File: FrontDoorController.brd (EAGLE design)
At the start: 31.4 x 49.1 mm, 11 parts

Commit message: Door_Control_PCB: Add SW3 and SW4 from Lockitron
The Lockitron has 4 limit switches instead of 2 like I originally
thought.  They also need a common place to wire their NC connections to
and with this many switches it seemed best to give them their own header
row, causing some other components to have to move and some other pins
to need moving as well.  Things all seem to flow well now and there
should be plenty of power to all of the components.
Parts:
- removed R1: 1K, SparkFun-Resistors:0603-RES
- added JP2: (no value), SparkFun-Connectors:1X04_LOCK
- moved D1 8.62 mm to (7.05, 6.98)
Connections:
- removed net A0: PHOTON.12, U$3.12
- removed net A1: PHOTON.11, U$3.11
- removed net VM: C1.A, C2.1, D1.A, JP1.6, U$2.13, U$2.14, U$2.24
- new net SW3: JP2.1, PHOTON.12, U$3.12
- new net SW4: JP2.2, PHOTON.11, U$3.11
- new net VBAK: PHOTON.22, U$3.22
- net DOORSW: no longer R1.2
- net GND: now also JP1.8, JP1.9; no longer R1.1
- net SW1: now also JP2.3; no longer JP1.8
- net SW2: now also JP2.4; no longer JP1.9
- net VBAT: now also C1.A, C2.1, D1.A, JP1.6, U$2.13, U$2.14, U$2.24; no longer PHOTON.22, U$3.22
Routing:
- net SW4: track 0.00 -> 33.2 mm, vias 0 -> 1
- net SW3: track 0.00 -> 22.4 mm
- net VM: track 14.2 -> 0.00 mm, vias 2 -> 0
- net VBAT: track 1.40 -> 14.2 mm, vias 0 -> 2
- net SW1: track 17.2 -> 12.1 mm
- net VIN: track 72.1 -> 76.6 mm
- net SW2: track 18.7 -> 15.5 mm
- net VBAK: track 0.00 -> 1.40 mm
- net A1: track 1.40 -> 0.00 mm
- net A0: track 1.38 -> 0.00 mm
- net DOORSW: track 25.0 -> 24.0 mm
- added copper zone on layer 1, net VBAT
- removed copper zone on layer 1, net VM
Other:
- board text added: "Door COM"
- board text added: "Door NC"
- board text added: "SW NC"
- board text added: "SW3"
- board text added: "SW4"
- board text added: "VBAT"
- board text removed: "DOORSW"
- board text removed: "VM"

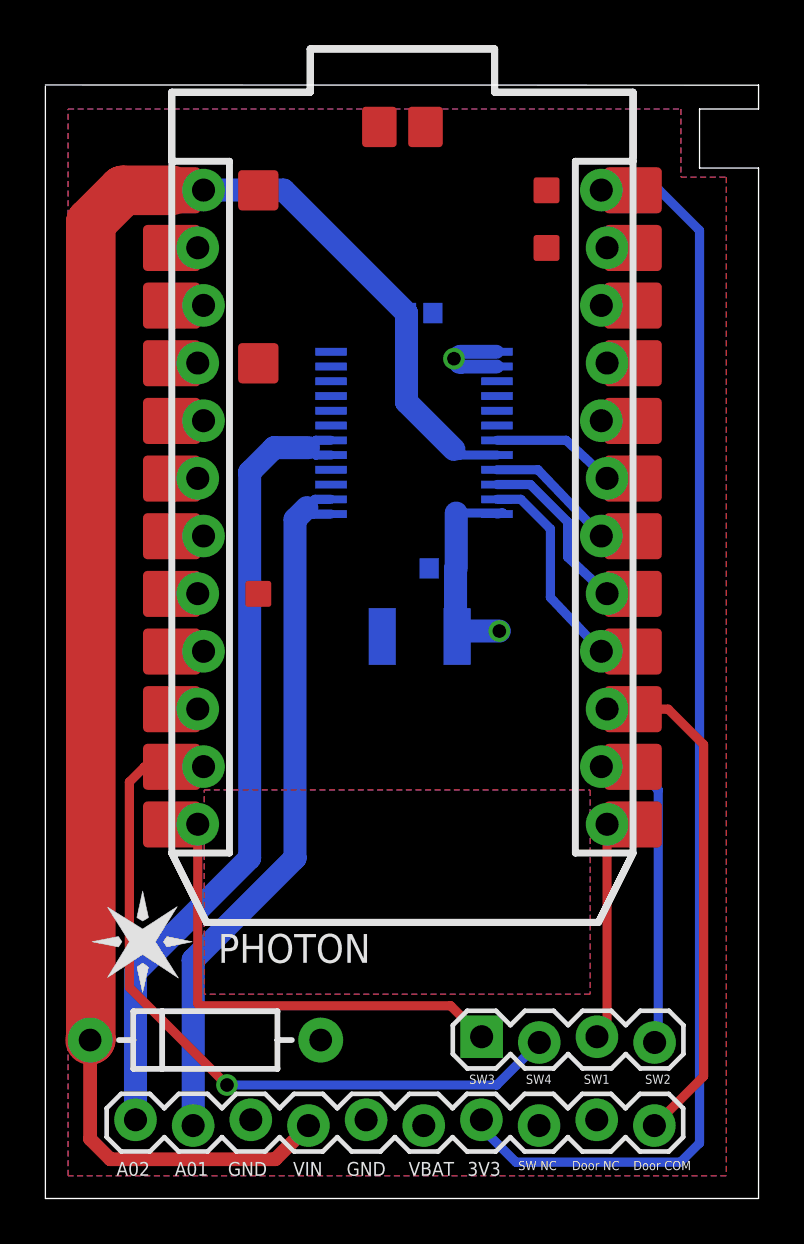
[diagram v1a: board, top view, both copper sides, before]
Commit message: Door_Control_PCB: Widen Motor A01/2 traces
These were probably wide enough but I thought that giving them as much
surface area as possible to transmit high current to the motor is a good
thing so I widened the traces by a bit.  This also made the connections
to the IC pads much prettier.
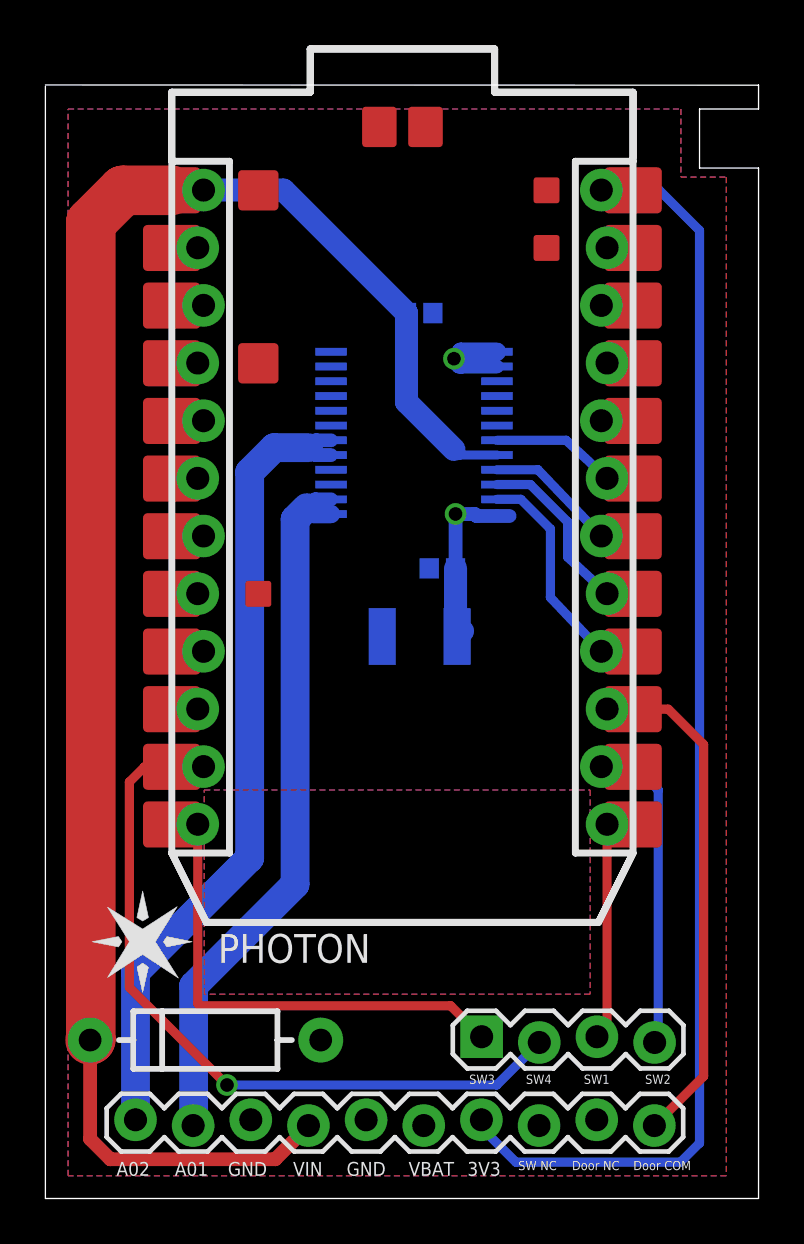
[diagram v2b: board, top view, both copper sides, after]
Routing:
- net VBAT: track 14.2 -> 13.2 mm
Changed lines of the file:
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@@
 <contactref element="U$2" pad="2"/>
 <contactref element="JP1" pad="2"/>
-<wire x1="12.584" y1="30.805" x2="11.885" y2="30.805" width="0.4064" layer="16"/>
-<wire x1="11.885" y1="30.805" x2="11.52" y2="30.44" width="0.4064" layer="16"/>
+<wire x1="12.584" y1="30.805" x2="11.885" y2="30.805" width="0.6096" layer="16"/>
+<wire x1="11.885" y1="30.805" x2="11.52" y2="30.44" width="0.6096" layer="16"/>
 <wire x1="11.52" y1="30.44" x2="11.805" y2="30.155" width="0.4064" layer="16"/>
-<wire x1="11.805" y1="30.155" x2="12.584" y2="30.155" width="0.4064" layer="16"/>
-<wire x1="6.51" y1="3.213" x2="6.51" y2="10.51" width="1.016" layer="16"/>
-<wire x1="6.51" y1="10.51" x2="11" y2="15" width="1.016" layer="16"/>
-<wire x1="11" y1="15" x2="11" y2="29.92" width="1.016" layer="16"/>
-<wire x1="11" y1="29.92" x2="11.52" y2="30.44" width="1.016" layer="16"/>
+<wire x1="11.805" y1="30.155" x2="12.584" y2="30.155" width="0.8128" layer="16"/>
+<wire x1="11" y1="13.84" x2="11" y2="29.92" width="1.27" layer="16"/>
+<wire x1="11" y1="29.92" x2="11.52" y2="30.44" width="1.27" layer="16"/>
+<wire x1="11" y1="13.84" x2="6.53" y2="9.37" width="1.27" layer="16"/>
+<wire x1="6.53" y1="9.37" x2="6.53" y2="3.233" width="1.27" layer="16"/>
+<wire x1="6.53" y1="3.233" x2="6.51" y2="3.213" width="1.27" layer="16"/>
 </signal>
 <signal name="A02">
@@
 <contactref element="U$2" pad="6"/>
 <contactref element="JP1" pad="1"/>
-<wire x1="12.584" y1="32.755" x2="11.915" y2="32.755" width="0.4064" layer="16"/>
-<wire x1="11.915" y1="32.755" x2="11.59" y2="33.08" width="0.4064" layer="16"/>
-<wire x1="11.59" y1="33.08" x2="11.915" y2="33.405" width="0.4064" layer="16"/>
-<wire x1="11.915" y1="33.405" x2="12.584" y2="33.405" width="0.4064" layer="16"/>
-<wire x1="3.97" y1="3.467" x2="3.97" y2="9.97" width="1.016" layer="16"/>
-<wire x1="3.97" y1="9.97" x2="9" y2="15" width="1.016" layer="16"/>
-<wire x1="9" y1="15" x2="9" y2="32" width="1.016" layer="16"/>
-<wire x1="9" y1="32" x2="10.08" y2="33.08" width="1.016" layer="16"/>
-<wire x1="10.08" y1="33.08" x2="11.59" y2="33.08" width="1.016" layer="16"/>
+<wire x1="12.584" y1="32.755" x2="11.915" y2="32.755" width="0.6096" layer="16"/>
+<wire x1="11.915" y1="32.755" x2="11.59" y2="33.08" width="0.6096" layer="16"/>
+<wire x1="11.59" y1="33.08" x2="11.915" y2="33.405" width="0.6096" layer="16"/>
+<wire x1="11.915" y1="33.405" x2="12.584" y2="33.405" width="0.6096" layer="16"/>
+<wire x1="3.97" y1="3.467" x2="3.97" y2="9.97" width="1.27" layer="16"/>
+<wire x1="3.97" y1="9.97" x2="9" y2="15" width="1.27" layer="16"/>
+<wire x1="9" y1="15" x2="9" y2="32" width="1.27" layer="16"/>
+<wire x1="9" y1="32" x2="10.08" y2="33.08" width="1.27" layer="16"/>
+<wire x1="10.08" y1="33.08" x2="11.59" y2="33.08" width="1.27" layer="16"/>
 </signal>
 <signal name="VBAT">
@@
 <wire x1="18.14" y1="24.76" x2="18.07" y2="24.76" width="0.4064" layer="16"/>
 <wire x1="18.07" y1="24.76" x2="18.07" y2="27.76" width="1.016" layer="16"/>
-<wire x1="18.07" y1="27.76" x2="18.1" y2="27.76" width="0.4064" layer="16"/>
-<wire x1="18.1" y1="27.76" x2="18.1" y2="30.2" width="1.016" layer="16"/>
-<wire x1="18.1" y1="30.2" x2="20.146" y2="30.2" width="0.4064" layer="16"/>
-<wire x1="20.146" y1="30.2" x2="19.896" y2="30.155" width="0.4064" layer="16"/>
 <wire x1="18.1" y1="36.685" x2="18.1" y2="36.76" width="0.4064" layer="16"/>
 <contactref element="D1" pad="A"/>
@@
 </polygon>
 <wire x1="18.14" y1="24.76" x2="18.38" y2="25" width="1.016" layer="16"/>
-<wire x1="18.38" y1="25" x2="20" y2="25" width="1.016" layer="16"/>
-<via x="20" y="25" extent="1-16" drill="0.6"/>
 <via x="18" y="37" extent="1-16" drill="0.6"/>
-<wire x1="19.896" y1="37.305" x2="18.305" y2="37.305" width="0.6096" layer="16"/>
-<wire x1="18.305" y1="37.305" x2="18" y2="37" width="0.6096" layer="16" curve="90"/>
+<wire x1="19.896" y1="37.305" x2="18.305" y2="37.305" width="0.8128" layer="16"/>
 <wire x1="19.896" y1="36.655" x2="18.345" y2="36.655" width="0.6096" layer="16"/>
 <wire x1="18.345" y1="36.655" x2="18" y2="37" width="0.6096" layer="16" curve="-90"/>
 <wire x1="18.345" y1="36.655" x2="18.205" y2="36.655" width="0.6096" layer="16"/>
-<wire x1="18.205" y1="36.655" x2="18.1" y2="36.76" width="0.6096" layer="16" curve="-90"/>
 <contactref element="JP1" pad="6"/>
+<wire x1="18.075" y1="30.155" x2="18.07" y2="30.16" width="0.6096" layer="16" curve="-90"/>
+<via x="18.07" y="30.16" extent="1-16" drill="0.6"/>
+<wire x1="18.07" y1="27.76" x2="18.07" y2="30.16" width="0.6096" layer="16"/>
+<wire x1="18.075" y1="30.155" x2="18.905" y2="30.155" width="0.6096" layer="16"/>
+<wire x1="18.905" y1="30.155" x2="18.99" y2="30.07" width="0.6096" layer="16" curve="-90"/>
+<wire x1="18.99" y1="30.07" x2="20.45" y2="30.07" width="0.6096" layer="16"/>
+<wire x1="20.45" y1="30.07" x2="19.981" y2="30.07" width="0.4064" layer="16"/>
+<wire x1="19.981" y1="30.07" x2="19.896" y2="30.155" width="0.4064" layer="16" curve="-90"/>
+<wire x1="18.305" y1="37.305" x2="18" y2="37" width="0.8128" layer="16" curve="-90"/>
+<wire x1="18.205" y1="36.655" x2="18.1" y2="36.76" width="0.6096" layer="16" curve="90"/>
 </signal>
 <signal name="N$3">
